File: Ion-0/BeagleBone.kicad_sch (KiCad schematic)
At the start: 3 parts, among them J1 Beaglebone-green-P9, J2 Beaglebone-green-P8

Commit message: fixes in the schematic, made it better
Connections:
- net GPIO-78: now reaches J2.37 (Pin_37)
- net GPIO-79: now reaches J2.38 (Pin_38)
- net GPIO-76: now reaches J2.39 (Pin_39)
- net GPIO-77: now reaches J2.40 (Pin_40)
- net GPIO-74: now reaches J2.41 (Pin_41)
- net GPIO-75: now reaches J2.42 (Pin_42)
- net GPIO-72: now reaches J2.43 (Pin_43)
- net GPIO-73: now reaches J2.44 (Pin_44)
- net CAN_RXD renamed CAN-RXD
- net CAN_TXD renamed CAN-TXD
- net GPIO_32 renamed GPIO-45
- net GPIO_36 renamed GPIO-69
- net GPIO_50 renamed GPIO-50
- net GPIO_51 renamed GPIO-51
- net GPIO_60 renamed GPIO-60
- net GPIO_62 renamed GPIO-47
- net GPIO_69 renamed GPIO-23
- net GPIO_72 renamed GPIO-46
- net GPIO_74 renamed GPIO-26
- net GPIO_76 renamed GPIO-44
- net GPIO_8 renamed GPIO-8
- net GPIO_86: no longer names the net of J2.17 (Pin_17)
- net I2C1_SCL renamed I2C1-SCL
- net I2C1_SDA renamed I2C1-SDA
- net IND_3 renamed GPIO-62
- net LED_PWM_1 renamed EHRPWM0A
- net LED_PWM_2 renamed EHRPWM2A
- net MOTOR_1_A renamed GPIO-86
- net MOTOR_1_B renamed GPIO-10
- net MOTOR_2_A renamed GPIO-36
- net MOTOR_2_B renamed GPIO-32
- net SERVO_1 renamed GPIO-87
- net SERVO_2 renamed GPIO-9
- net ~{SYS_RST} renamed ~{SYS-RST}
- no-connect marks 44 -> 40
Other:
- moved on the sheet: C23

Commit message: BUZZER NEVER DIES
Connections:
- net GPIO-27: now reaches J2.17 (Pin_17)
- no-connect marks 40 -> 39
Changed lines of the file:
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@@
-	)
-	(no_connect
-		(at 175.26 77.47)
 	)
 	(no_connect
@@
 	(wire
 		(pts
+			(xy 172.72 77.47) (xy 175.26 77.47)
+		)
+		(stroke
+			(width 0)
+			(type default)
+		)
+	)
+	(wire
+		(pts
 			(xy 137.16 95.25) (xy 137.16 93.98)
 		)
@@
 		(effects
 			(font
+				(size 1.27 1.27)
+			)
+			(justify right)
+		)
+	)
+	(hierarchical_label "GPIO-27"
+		(shape input)
+		(at 172.72 77.47 180)
+		(effects
+			(font

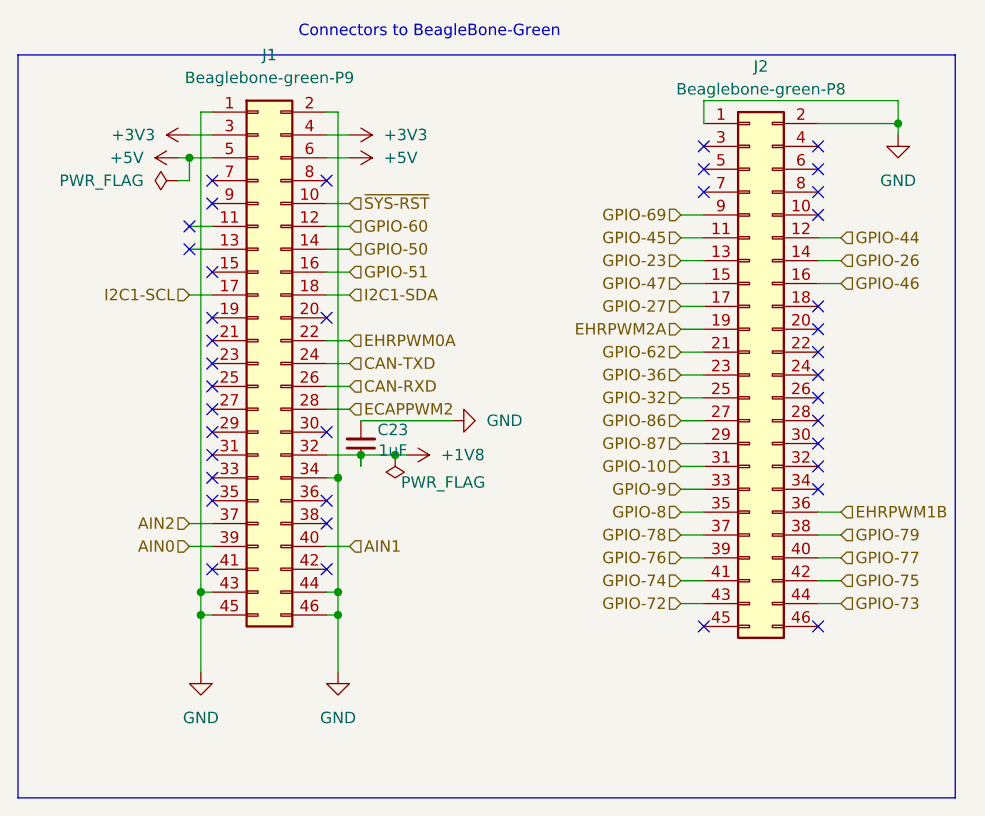
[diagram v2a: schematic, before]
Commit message: version 0.8 - stepper driver included and better detailled schematic
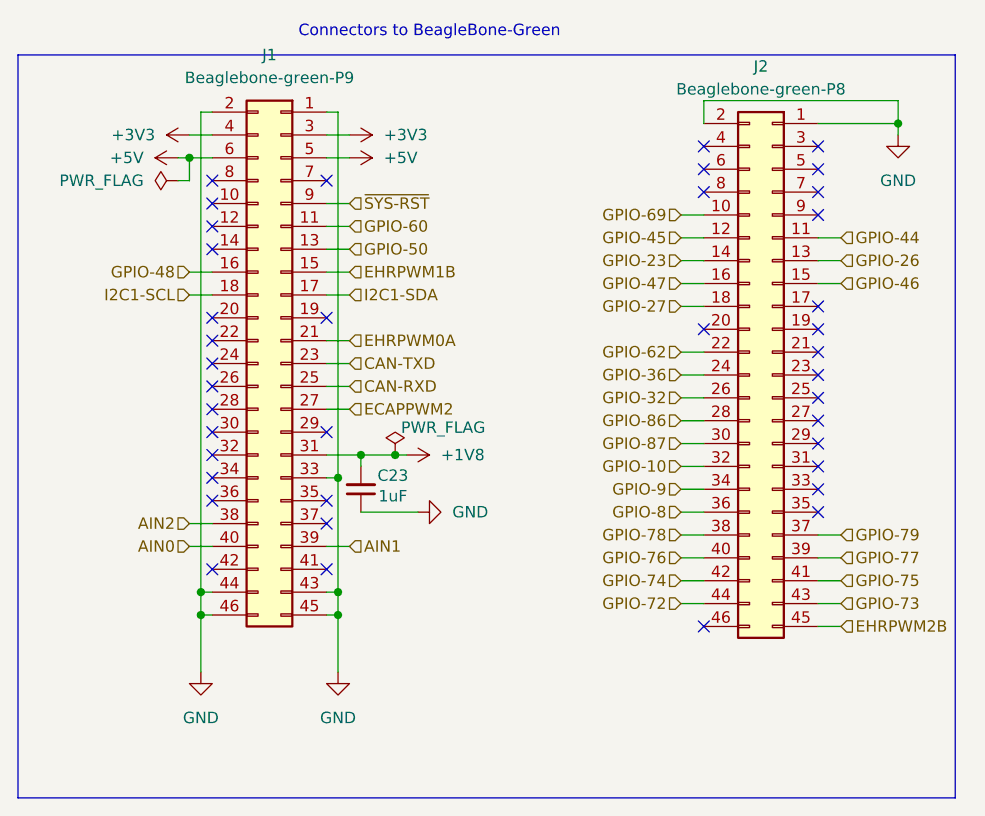
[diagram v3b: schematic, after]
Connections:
- net +1V8: now also C23.2, J1.31 (Pin_31); no longer C23.1, J1.32 (Pin_32)
- net AIN0: now also J1.40 (Pin_40); no longer J1.39 (Pin_39)
- net AIN1: now also J1.39 (Pin_39); no longer J1.40 (Pin_40)
- net AIN2: now also J1.38 (Pin_38); no longer J1.37 (Pin_37)
- net CAN-RXD: now also J1.25 (Pin_25); no longer J1.26 (Pin_26)
- net CAN-TXD: now also J1.23 (Pin_23); no longer J1.24 (Pin_24)
- net ECAPPWM2: now also J1.27 (Pin_27); no longer J1.28 (Pin_28)
- net EHRPWM0A: now also J1.21 (Pin_21); no longer J1.22 (Pin_22)
- net EHRPWM1B: now also J1.15 (Pin_15); no longer J2.36 (Pin_36)
- net GND: now also C23.1, J1.33 (Pin_33); no longer C23.2, J1.34 (Pin_34)
- net GPIO-10: now also J2.32 (Pin_32); no longer J2.31 (Pin_31)
- net GPIO-23: now also J2.14 (Pin_14); no longer J2.13 (Pin_13)
- net GPIO-26: now also J2.13 (Pin_13); no longer J2.14 (Pin_14)
- net GPIO-27: now also J2.18 (Pin_18); no longer J2.17 (Pin_17)
- net GPIO-32: now also J2.26 (Pin_26); no longer J2.25 (Pin_25)
- net GPIO-36: now also J2.24 (Pin_24); no longer J2.23 (Pin_23)
- net GPIO-44: now also J2.11 (Pin_11); no longer J2.12 (Pin_12)
- net GPIO-45: now also J2.12 (Pin_12); no longer J2.11 (Pin_11)
- net GPIO-46: now also J2.15 (Pin_15); no longer J2.16 (Pin_16)
- net GPIO-47: now also J2.16 (Pin_16); no longer J2.15 (Pin_15)
- net GPIO-50: now also J1.13 (Pin_13); no longer J1.14 (Pin_14)
- net GPIO-60: now also J1.11 (Pin_11); no longer J1.12 (Pin_12)
- net GPIO-62: now also J2.22 (Pin_22); no longer J2.21 (Pin_21)
- net GPIO-69: now also J2.10 (Pin_10); no longer J2.9 (Pin_9)
- net GPIO-72: now also J2.44 (Pin_44); no longer J2.43 (Pin_43)
- net GPIO-73: now also J2.43 (Pin_43); no longer J2.44 (Pin_44)
- net GPIO-74: now also J2.42 (Pin_42); no longer J2.41 (Pin_41)
- net GPIO-75: now also J2.41 (Pin_41); no longer J2.42 (Pin_42)
- net GPIO-76: now also J2.40 (Pin_40); no longer J2.39 (Pin_39)
- net GPIO-77: now also J2.39 (Pin_39); no longer J2.40 (Pin_40)
- net GPIO-78: now also J2.38 (Pin_38); no longer J2.37 (Pin_37)
- net GPIO-79: now also J2.37 (Pin_37); no longer J2.38 (Pin_38)
- net GPIO-8: now also J2.36 (Pin_36); no longer J2.35 (Pin_35)
- net GPIO-86: now also J2.28 (Pin_28); no longer J2.27 (Pin_27)
- net GPIO-87: now also J2.30 (Pin_30); no longer J2.29 (Pin_29)
- net GPIO-9: now also J2.34 (Pin_34); no longer J2.33 (Pin_33)
- net I2C1-SCL: now also J1.18 (Pin_18); no longer J1.17 (Pin_17)
- net I2C1-SDA: now also J1.17 (Pin_17); no longer J1.18 (Pin_18)
- net ~{SYS-RST}: now also J1.9 (Pin_9); no longer J1.10 (Pin_10)
- net EHRPWM2B: now reaches J2.45 (Pin_45)
- net EHRPWM2A: no longer names the net of J2.19 (Pin_19)
- net GPIO-51 renamed GPIO-48
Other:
- moved on the sheet: C23
